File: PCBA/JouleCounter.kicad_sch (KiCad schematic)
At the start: 2 parts

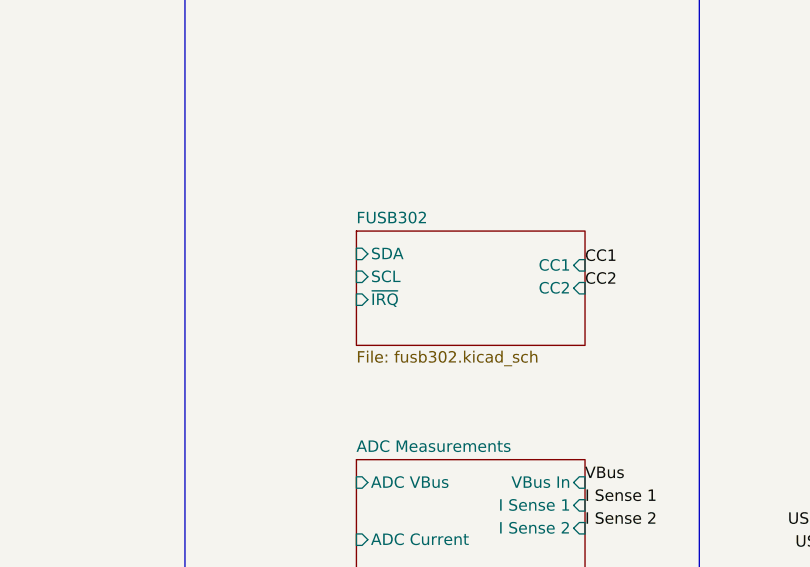
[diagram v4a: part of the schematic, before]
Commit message: TODO: usb c plug
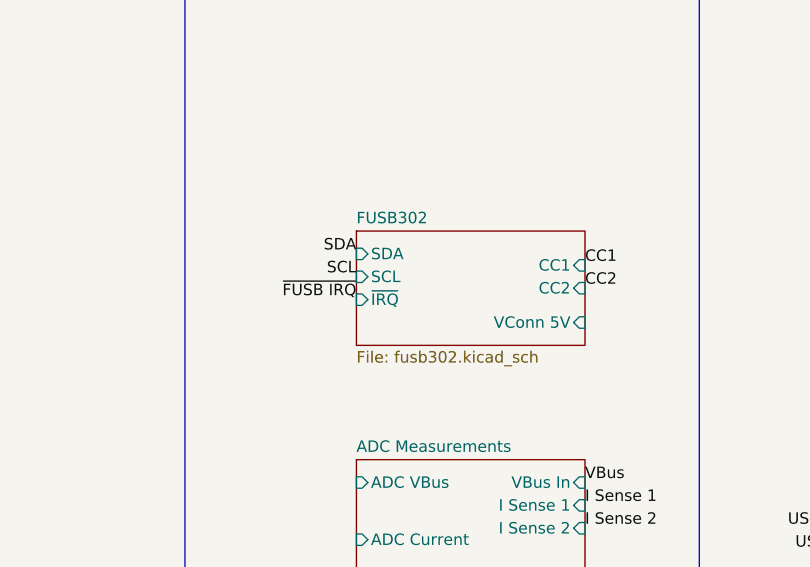
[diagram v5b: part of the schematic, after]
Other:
- sheet FUSB302 ports: added VConn 5V; removed none
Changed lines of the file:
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@@
     (effects (font (size 1.27 1.27)) (justify left bottom))
+  )
+  (label "SCL" (at 190.5 55.88 180)
+    (effects (font (size 1.27 1.27)) (justify right bottom))
   )
   (label "CC2" (at 254 81.28 180)
@@
     (effects (font (size 1.27 1.27)) (justify left bottom))
   )
+  (label "~{FUSB IRQ}" (at 190.5 58.42 180)
+    (effects (font (size 1.27 1.27)) (justify right bottom))
+  )
   (label "BootMode" (at 262.89 152.4 0)
     (effects (font (size 1.27 1.27)) (justify left bottom))
@@
   )
   (label "BootMode" (at 254 115.57 180)
+    (effects (font (size 1.27 1.27)) (justify right bottom))
+  )
+  (label "SDA" (at 190.5 53.34 180)
     (effects (font (size 1.27 1.27)) (justify right bottom))
   )
@@
       (effects (font (size 1.27 1.27)) (justify left))
     )
+    (pin "VConn 5V" input (at 215.9 60.96 0)
+      (effects (font (size 1.27 1.27)) (justify right))
+    )
   )
   (sheet (at 254 101.6) (size 25.4 25.4) (fields_autoplaced)
@@
       (reference "L201") (unit 1) (value "2.2uH") (footprint "")
     )
+    (path "/11e6ad7b-94c7-4abc-98e0-e4b10d097f65/baceac92-88cf-4c29-a2b6-9336e798c4e5"
+      (reference "P?") (unit 1) (value "USB_C_Plug") (footprint "")
+    )
     (path "/4847c8c0-6173-45c5-9b4b-8c9418cb5a91/271287de-d1ab-46e7-9e8d-0eca17ee0aae"

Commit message: More schematics
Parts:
- removed SW?: SW_Push, symbol Switch:SW_Push
- gave numbers to parts that had none: 1
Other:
- removed sheet Flash
- added sheet UI (ui.kicad_sch)
- note added: "User Interface"
